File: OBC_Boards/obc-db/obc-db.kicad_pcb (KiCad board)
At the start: 4 copper layers, 90.2 x 95.9 mm, 57 parts, among them J1 PC104_Connector, J2 Raspberry Pi 4 Connector, J3 Temp Sens1 Connector, J4 Test Connector, J5 Temp Sens2 Connector, J6 ST11S008V4HR2000, U1 L102021MS02Q, U2 AZ1117IH-3.3TRG1, U3 MCP3008-I/SL, U4 MAX4372FESA+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

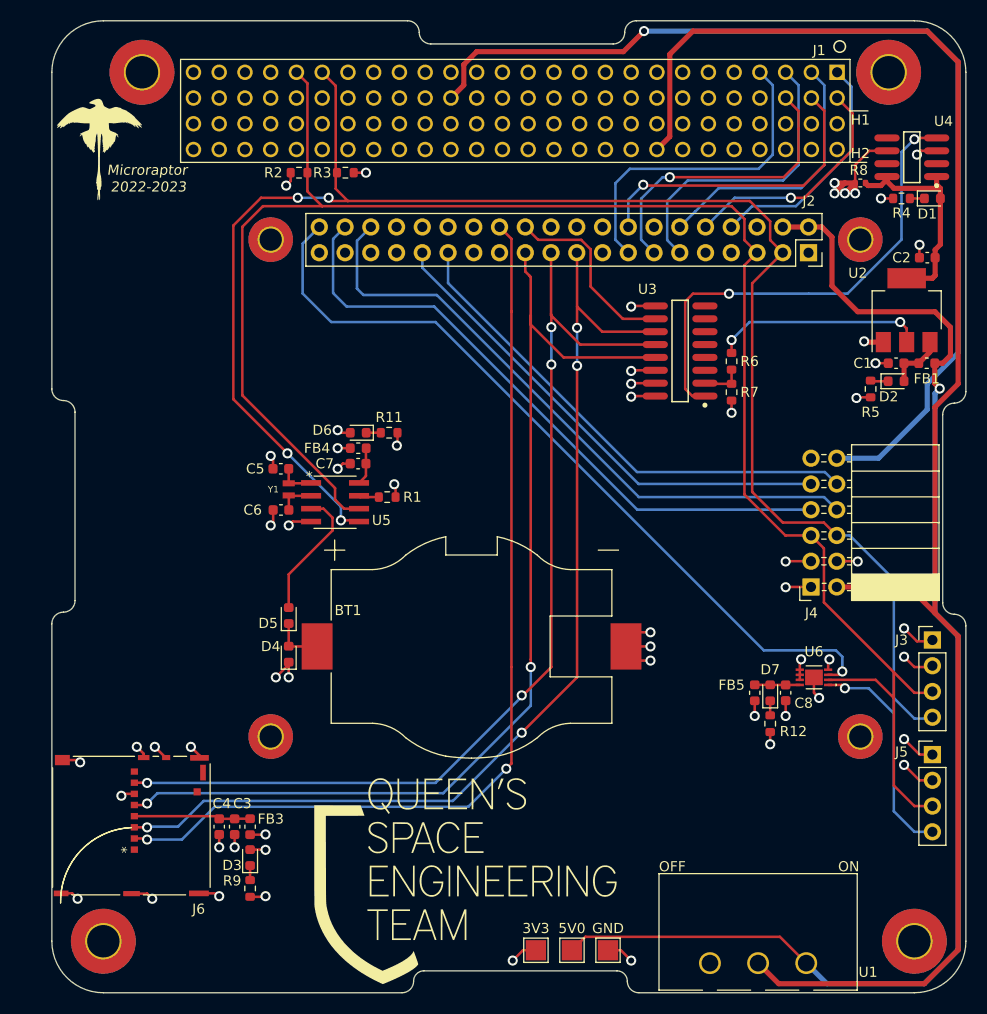
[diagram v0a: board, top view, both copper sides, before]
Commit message: new microSD connector
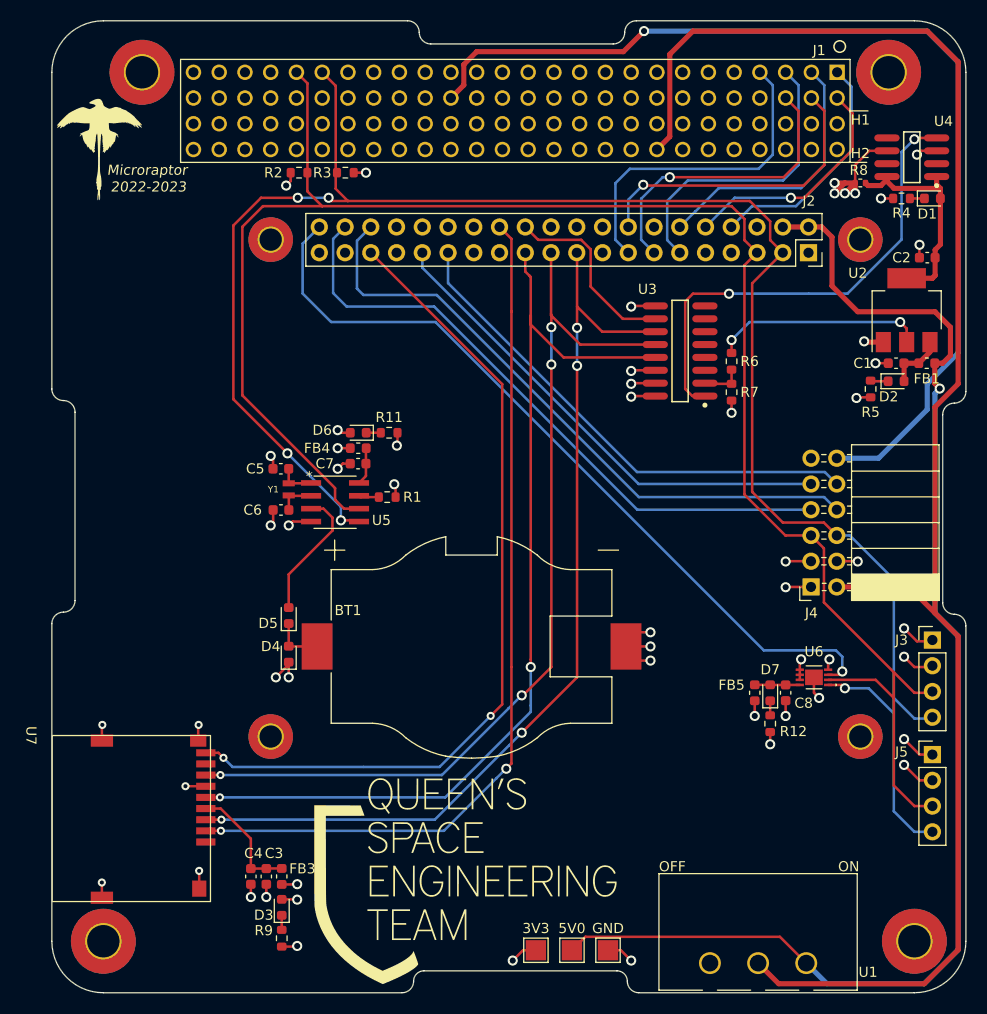
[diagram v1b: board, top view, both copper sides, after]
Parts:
- removed J6: ST11S008V4HR2000, qset-footprints:ST11S008V4HR2000
- added U7: MR01A-01211, qset-footprints:MR01A-01211, F.Cu at (109.2, 117.5)
- moved D3 5.82 mm to (131.9, 134.4)
- moved R9 5.82 mm to (131.9, 137.5)
- moved FB3 5.82 mm to (131.9, 131.4)
- moved C3 5.82 mm to (130.4, 131.4)
- moved C4 5.82 mm to (128.9, 131.4)
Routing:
- net GPIO19: track 0.00 -> 82.3 mm, vias 0 -> 2
- net SPI1_CE1_N: track 93.8 -> 86.3 mm
- net SPI1_MISO: track 98.3 -> 91.0 mm
- net SPI1_MOSI: track 100.4 -> 93.1 mm
- net SPI1_CLK: track 102.6 -> 95.6 mm
- net GND: track 106.9 -> 101.6 mm, vias 38 -> 35
- net Net-(C3-Pad1): track 11.5 -> 12.0 mm

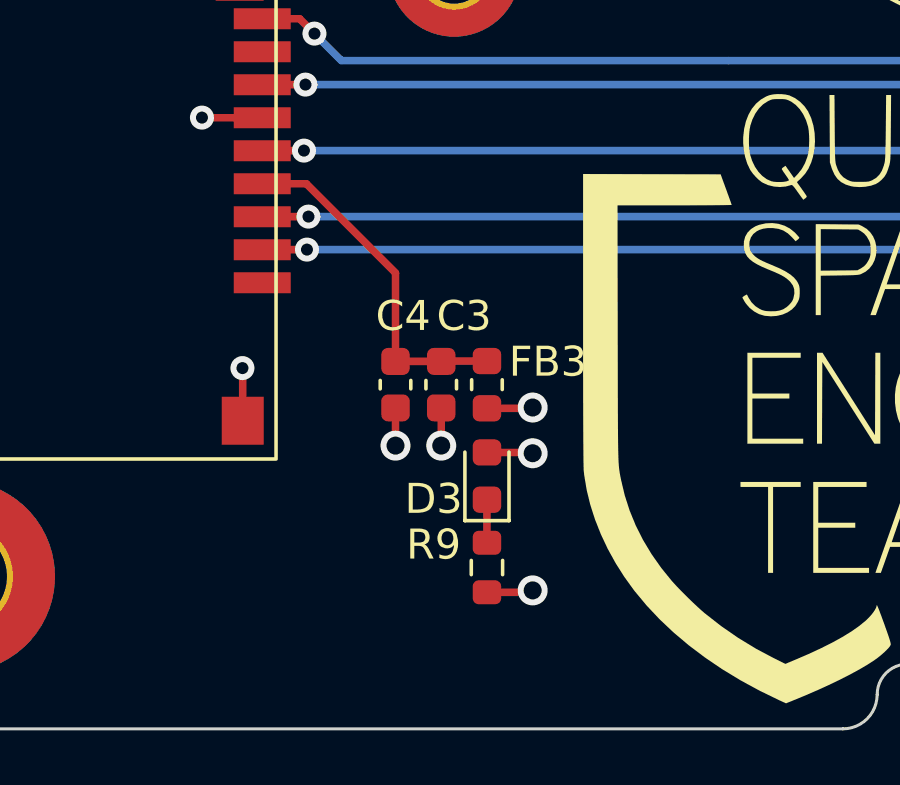
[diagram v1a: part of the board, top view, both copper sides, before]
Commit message: new microSD
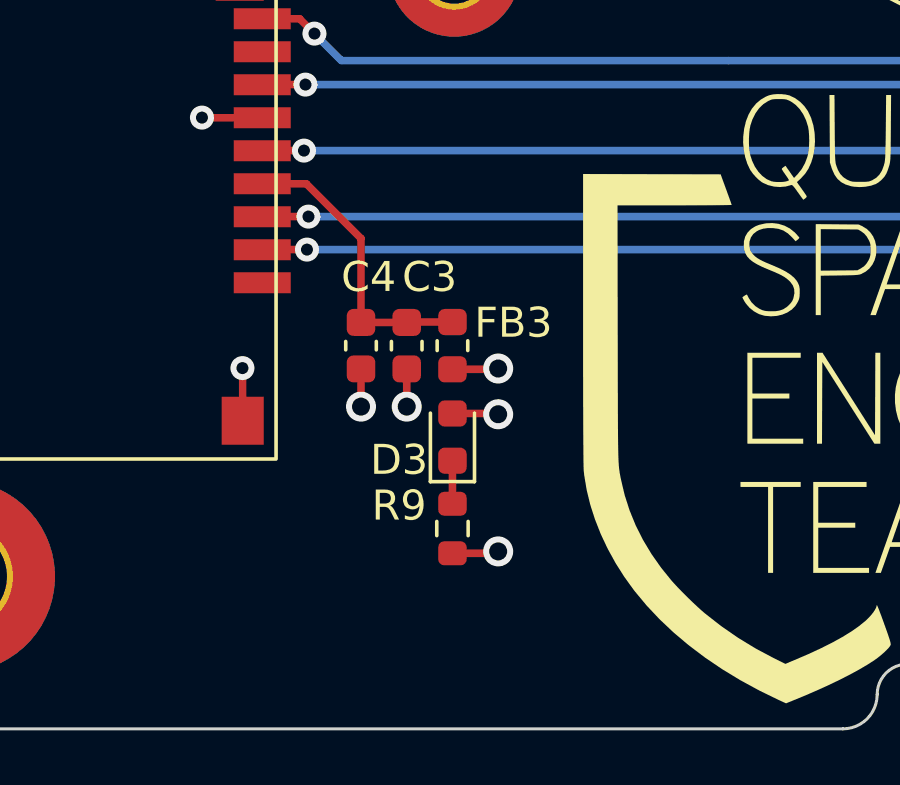
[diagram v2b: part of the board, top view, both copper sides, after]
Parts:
- moved C3 1.74 mm to (129.2, 130.1)
- moved C4 1.74 mm to (127.7, 130.1)
- moved D3 1.74 mm to (130.8, 133.2)
- moved FB3 1.74 mm to (130.8, 130.1)
- moved R9 1.74 mm to (130.8, 136.2)
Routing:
- net Net-(C3-Pad1): track 12.0 -> 10.3 mm

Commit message: OBC: obc-db: remove redundant .DS_Store files
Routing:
- net GND: track 101.6 -> 84.9 mm
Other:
- board text added: "TEST"
- board text added: "TP-SENS1"
- board text added: "TP-SENS2"
- board text removed: "2022-2023"
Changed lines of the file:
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@@
     (fp_arc (start -6.5 -9) (mid -7.988267 -7.977054) (end -9.75 -7.58) (layer "F.SilkS") (width 0.127))
     (fp_arc (start -6.5 -9) (mid -4.626324 -10.143582) (end -2.54 -10.826) (layer "F.SilkS") (width 0.127))
-    (fp_arc (start 9.75 -7.58) (mid 7.988267 -7.977054) (end 6.5 -9) (layer "F.SilkS") (width 0.127))
+    (fp_arc (start 9.75 -7.58) (mid 7.988266 -7.977054) (end 6.5 -9) (layer "F.SilkS") (width 0.127))
     (fp_arc (start -2.54 10.826) (mid -4.626324 10.143582) (end -6.5 9) (layer "F.SilkS") (width 0.127))
     (fp_arc (start -9.75 7.58) (mid -7.988267 7.977054) (end -6.5 9) (layer "F.SilkS") (width 0.127))
     (fp_arc (start 2.54 -10.826) (mid 4.626324 -10.143582) (end 6.5 -9) (layer "F.SilkS") (width 0.127))
     (fp_arc (start 2.54 10.826) (mid 1.27297 10.961886) (end 0 11.02) (layer "F.SilkS") (width 0.127))
-    (fp_arc (start 6.5 9) (mid 7.988267 7.977054) (end 9.75 7.58) (layer "F.SilkS") (width 0.127))
+    (fp_arc (start 6.5 9) (mid 7.988266 7.977054) (end 9.75 7.58) (layer "F.SilkS") (width 0.127))
     (fp_arc (start 0 11.02) (mid -1.27297 10.961886) (end -2.54 10.826) (layer "F.SilkS") (width 0.127))
     (fp_line (start 17.01 -11.27) (end 17.01 11.27) (layer "F.CrtYd") (width 0.05))
@@
     (fp_arc (start 0 11.02) (mid -1.27297 10.961886) (end -2.54 10.826) (layer "F.Fab") (width 0.127))
     (fp_arc (start 2.54 -10.826) (mid 4.626324 -10.143582) (end 6.5 -9) (layer "F.Fab") (width 0.127))
-    (fp_arc (start 6.5 9) (mid 7.988267 7.977054) (end 9.75 7.58) (layer "F.Fab") (width 0.127))
+    (fp_arc (start 6.5 9) (mid 7.988266 7.977054) (end 9.75 7.58) (layer "F.Fab") (width 0.127))
     (fp_arc (start -6.5 -9) (mid -4.626324 -10.143582) (end -2.54 -10.826) (layer "F.Fab") (width 0.127))
     (fp_arc (start 6.5 9) (mid 4.626324 10.143582) (end 2.54 10.826) (layer "F.Fab") (width 0.127))
     (fp_arc (start 2.54 10.826) (mid 1.27297 10.961886) (end 0 11.02) (layer "F.Fab") (width 0.127))
-    (fp_arc (start 9.75 -7.58) (mid 7.988267 -7.977054) (end 6.5 -9) (layer "F.Fab") (width 0.127))
+    (fp_arc (start 9.75 -7.58) (mid 7.988266 -7.977054) (end 6.5 -9) (layer "F.Fab") (width 0.127))
     (fp_poly (pts
         (xy -3 -2)
@@
     (property "Sheetname" "")
     (attr through_hole)
-    (fp_text reference "J3" (at -3.048 0 180) (layer "F.SilkS")
+    (fp_text reference "J3" (at 0.0508 -2.3622 180) (layer "F.SilkS")
       (effects (font (size 1 1) (thickness 0.15)))
     )
@@
     (property "Sheetname" "micro-sd-card-reader")
     (attr smd)
-    (fp_text reference "U7" (at 0 2.08 -90 unlocked) (layer "F.SilkS")
+    (fp_text reference "U7" (at -0.914 -1.24 unlocked) (layer "F.SilkS")
       (effects (font (size 1 1) (thickness 0.15)))
     )
@@
     (property "Sheetname" "")
     (attr through_hole)
-    (fp_text reference "J5" (at -3.048 -0.264 180) (layer "F.SilkS")
+    (fp_text reference "J5" (at 0 10.0584 180) (layer "F.SilkS")
       (effects (font (size 1 1) (thickness 0.15)))
     )
@@
     (effects (font (size 1 1) (thickness 0.15)))
   )
-  (gr_text "2022-2023" (at 118.745 63.373) (layer "F.SilkS")
-    (effects (font (size 1 1) (thickness 0.15) italic))
-  )
   (gr_text "Microraptor" (at 118.618 61.722) (layer "F.SilkS")
     (effects (font (size 1 1) (thickness 0.15) italic))
   )
+  (gr_text "TEST" (at 189.6872 87.63) (layer "F.SilkS")
+    (effects (font (size 1 1) (thickness 0.15)))
+  )
+  (gr_text "TP-SENS2" (at 193.3956 124.8156 90) (layer "F.SilkS")
+    (effects (font (size 1 1) (thickness 0.15)))
+  )
+  (gr_text "TP-SENS1" (at 193.6496 113.3348 90) (layer "F.SilkS")
+    (effects (font (size 1 1) (thickness 0.15)))
+  )
   (dimension (type aligned) (layer "F.Fab")
     (pts (xy 109.22 142.875) (xy 109.22 137.795))
@@
   (segment (start 123.658 118.005) (end 123.658 116.492) (width 0.25) (layer "F.Cu") (net 61))
   (segment (start 132.211 137.023) (end 132.274 136.96) (width 0.254) (layer "F.Cu") (net 61))
-  (segment (start 194.31 110.744) (end 193.294 109.728) (width 0.254) (layer "F.Cu") (net 61))
   (segment (start 183.007 112.00965) (end 183.007 111.50965) (width 0.254) (layer "F.Cu") (net 61))
   (segment (start 167.254 107.315) (end 168.275 107.315) (width 0.254) (layer "F.Cu") (net 61))
@@
   (segment (start 114.158 132.008) (end 114.15 132) (width 0.25) (layer "F.Cu") (net 61))
   (segment (start 122.405 122.505) (end 122.4 122.5) (width 0.25) (layer "F.Cu") (net 61))
+  (segment (start 194.31 110.744) (end 193.548 109.982) (width 0.254) (layer "F.Cu") (net 61))
   (segment (start 180.086 117.157) (end 180.086 118.364) (width 0.254) (layer "F.Cu") (net 61))
   (segment (start 165.354 138.684) (end 166.37 139.7) (width 0.254) (layer "F.Cu") (net 61))
   (segment (start 165.857 108.712) (end 167.254 107.315) (width 0.254) (layer "F.Cu") (net 61))
+  (segment (start 193.548 109.982) (end 193.548 109.22) (width 0.254) (layer "F.Cu") (net 61))
   (segment (start 176.276 84.454) (end 176.276 85.661) (width 0.254) (layer "F.Cu") (net 61))
-  (via (at 193.294 109.728) (size 1) (drill 0.6) (layers "F.Cu" "B.Cu") (net 61))
   (via (at 193.294 120.396) (size 1) (drill 0.6) (layers "F.Cu" "B.Cu") (net 61))
   (via (at 143.256 88.9) (size 1) (drill 0.6) (layers "F.Cu" "B.Cu") (net 61))
@@
   (via (at 132.274 136.96) (size 1) (drill 0.6) (layers "F.Cu" "B.Cu") (net 61))
   (via (at 189.357 78.613) (size 1) (drill 0.6) (layers "F.Cu" "B.Cu") (net 61))
+  (via (at 193.548 109.22) (size 1) (drill 0.6) (layers "F.Cu" "B.Cu") (net 61))
   (via (at 188.722 100.33) (size 1) (drill 0.6) (layers "F.Cu" "B.Cu") (net 61))
   (via (at 114.2 116.45) (size 0.8) (drill 0.4) (layers "F.Cu" "B.Cu") (net 61))
@@
   (via (at 166.37 81.534) (size 1) (drill 0.6) (layers "F.Cu" "B.Cu") (net 61))
   (via (at 184.912 113.792) (size 1) (drill 0.6) (layers "F.Cu" "B.Cu") (net 61))
-  (segment (start 161.29 57.15) (end 162.379 56.061) (width 0.254) (layer "In1.Cu") (net 61))
   (segment (start 175.090259 58.589741) (end 172.550259 58.589741) (width 0.254) (layer "In1.Cu") (net 61))
   (segment (start 162.379 58.239) (end 161.29 57.15) (width 0.254) (layer "In1.Cu") (net 61))
   (segment (start 171.45 59.69) (end 170.361 58.601) (width 0.254) (layer "In1.Cu") (net 61))
-  (segment (start 165.281 56.061) (end 166.37 57.15) (width 0.254) (layer "In1.Cu") (net 61))
-  (segment (start 176.53 57.15) (end 175.441 56.061) (width 0.254) (layer "In1.Cu") (net 61))
   (segment (start 166.37 57.15) (end 165.281 58.239) (width 0.254) (layer "In1.Cu") (net 61))
-  (segment (start 162.379 56.061) (end 165.281 56.061) (width 0.254) (layer "In1.Cu") (net 61))
   (segment (start 165.281 58.239) (end 162.379 58.239) (width 0.254) (layer "In1.Cu") (net 61))
   (segment (start 176.53 57.15) (end 175.090259 58.589741) (width 0.254) (layer "In1.Cu") (net 61))
@@
   (segment (start 170.361 58.601) (end 167.821 58.601) (width 0.254) (layer "In1.Cu") (net 61))
   (segment (start 172.550259 58.589741) (end 171.45 59.69) (width 0.254) (layer "In1.Cu") (net 61))
-  (segment (start 167.459 56.061) (end 166.37 57.15) (width 0.254) (layer "In1.Cu") (net 61))
-  (segment (start 175.441 56.061) (end 167.459 56.061) (width 0.254) (layer "In1.Cu") (net 61))
   (segment (start 195.58 48.006) (end 198.628 51.054) (width 0.508) (layer "F.Cu") (net 65))
   (segment (start 198.628 138.644537) (end 195.286537 141.986) (width 0.508) (layer "F.Cu") (net 65))
